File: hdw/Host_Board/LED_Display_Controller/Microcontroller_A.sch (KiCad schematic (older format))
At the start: 1 part

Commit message: Added a few missing pages
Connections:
- net labels added: GND
- wire segments 0 -> 2
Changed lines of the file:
@@
 $Descr A 11000 8500
 encoding utf-8
-Sheet 13 20
+Sheet 13 24
 Title ""
 Date ""
@@
 NoConn ~ 7130 5380
 NoConn ~ 7130 5480
+$Comp
+L power:GND #PWR?
+U 1 1 5BB53596
+P 7320 5380
+F 0 "#PWR?" H 7320 5130 50  0001 C CNN
+F 1 "GND" H 7320 5230 50  0000 C CNN
+F 2 "" H 7320 5380 50  0001 C CNN
+F 3 "" H 7320 5380 50  0001 C CNN
+	1    7320 5380
+	1    0    0    -1
+$EndComp
+Wire Wire Line
+	7320 5380 7320 5280
+Wire Wire Line
+	7320 5280 7130 5280
 $EndSCHEMATC

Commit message: Wired Micro to external SRAM, copied Flash 8 times
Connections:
- net labels added: EBI_A10, EBI_A12, EBI_A14, EBI_A15, EBI_A5, EBI_A6, EBI_A7, EBI_IO0, EBI_IO1, EBI_IO12, EBI_IO13, EBI_IO14, EBI_IO15, EBI_IO2, EBI_IO3, EBI_IO4, EBI_IO5, EBI_IO6, EBI_IO7, FLASH_MISO, FLASH_MOSI, FLASH_SCK, ICSPCLK, ICSPDAT, ~EBI_OE, ~EBI_WE, ~FLASH_CE1, ~FLASH_CE2, ~FLASH_CE3, ~FLASH_CE4, ~FLASH_CE5, ~FLASH_CE6, ~FLASH_CE7, ~FLASH_CE8, ~FLASH_Hold
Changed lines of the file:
@@
 Wire Wire Line
 	7320 5280 7130 5280
+Text GLabel 4030 2980 0    50   BiDi ~ 0
+ICSPDAT
+Text GLabel 4030 3080 0    50   Input ~ 0
+ICSPCLK
+Text GLabel 4030 2080 0    50   Output ~ 0
+EBI_A5
+Text GLabel 4030 4780 0    50   Output ~ 0
+EBI_A6
+Text GLabel 4030 3880 0    50   Output ~ 0
+EBI_A7
+Text GLabel 4030 3780 0    50   Output ~ 0
+EBI_A10
+Text GLabel 4030 4880 0    50   Output ~ 0
+EBI_A12
+Text GLabel 4030 1980 0    50   Output ~ 0
+EBI_A14
+Text GLabel 7130 2380 2    50   Output ~ 0
+EBI_A15
+Text GLabel 7130 3280 2    50   BiDi ~ 0
+EBI_IO0
+Text GLabel 7130 3380 2    50   BiDi ~ 0
+EBI_IO1
+Text GLabel 7130 3480 2    50   BiDi ~ 0
+EBI_IO2
+Text GLabel 7130 3580 2    50   BiDi ~ 0
+EBI_IO3
+Text GLabel 7130 3680 2    50   BiDi ~ 0
+EBI_IO4
+Text GLabel 7130 3780 2    50   BiDi ~ 0
+EBI_IO5
+Text GLabel 7130 3880 2    50   BiDi ~ 0
+EBI_IO6
+Text GLabel 7130 3980 2    50   BiDi ~ 0
+EBI_IO7
+Text GLabel 7130 2680 2    50   BiDi ~ 0
+EBI_IO12
+Text GLabel 7130 2780 2    50   BiDi ~ 0
+EBI_IO13
+Text GLabel 7130 1780 2    50   BiDi ~ 0
+EBI_IO14
+Text GLabel 7130 1880 2    50   BiDi ~ 0
+EBI_IO15
+Text GLabel 4030 4980 0    40   Output ~ 0
+~EBI_WE
+Text GLabel 4030 5080 0    40   Input ~ 0
+~EBI_OE
+Text GLabel 1130 3390 0    40   Input ~ 0
+~FLASH_Hold
+Text GLabel 1130 4150 0    50   Input ~ 0
+FLASH_SCK
+Text GLabel 1260 2420 0    40   Input ~ 0
+~FLASH_CE1
+Text GLabel 1130 3750 0    50   Input ~ 0
+FLASH_MOSI
+Text GLabel 660  4860 2    50   Output ~ 0
+FLASH_MISO
+Text GLabel 1260 2520 0    40   Input ~ 0
+~FLASH_CE2
+Text GLabel 1260 2620 0    40   Input ~ 0
+~FLASH_CE3
+Text GLabel 1260 2720 0    40   Input ~ 0
+~FLASH_CE4
+Text GLabel 1260 2820 0    40   Input ~ 0
+~FLASH_CE5
+Text GLabel 1260 2920 0    40   Input ~ 0
+~FLASH_CE6
+Text GLabel 1260 3020 0    40   Input ~ 0
+~FLASH_CE7
+Text GLabel 1260 3120 0    40   Input ~ 0
+~FLASH_CE8
 $EndSCHEMATC

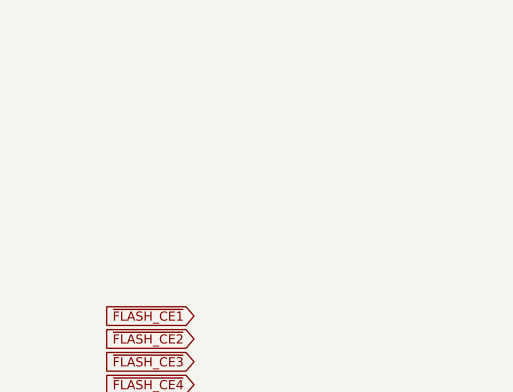
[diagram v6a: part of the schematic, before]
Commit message: Added to-do list, cleaned some pages, ~MCLR filter
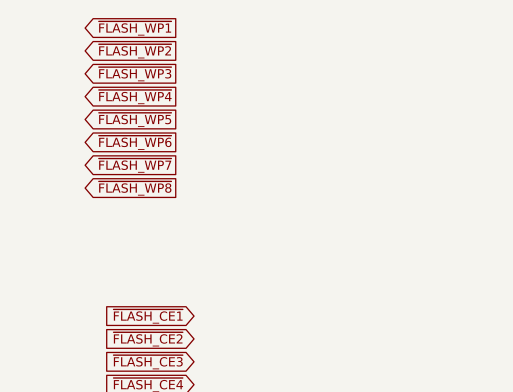
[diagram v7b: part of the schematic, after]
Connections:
- net labels added: ~FLASH_WP1, ~FLASH_WP2, ~FLASH_WP3, ~FLASH_WP4, ~FLASH_WP5, ~FLASH_WP6, ~FLASH_WP7, ~FLASH_WP8
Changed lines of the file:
@@
 $Descr A 11000 8500
 encoding utf-8
-Sheet 13 25
+Sheet 11 25
 Title ""
 Date ""
@@
 Text GLabel 1260 3120 0    40   Input ~ 0
 ~FLASH_CE8
+Text GLabel 1180 1160 0    40   Output ~ 0
+~FLASH_WP1
+Text GLabel 1180 1260 0    40   Output ~ 0
+~FLASH_WP2
+Text GLabel 1180 1360 0    40   Output ~ 0
+~FLASH_WP3
+Text GLabel 1180 1460 0    40   Output ~ 0
+~FLASH_WP4
+Text GLabel 1180 1560 0    40   Output ~ 0
+~FLASH_WP5
+Text GLabel 1180 1660 0    40   Output ~ 0
+~FLASH_WP6
+Text GLabel 1180 1760 0    40   Output ~ 0
+~FLASH_WP7
+Text GLabel 1180 1860 0    40   Output ~ 0
+~FLASH_WP8
 $EndSCHEMATC
